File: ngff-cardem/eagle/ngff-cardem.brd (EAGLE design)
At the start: 90 x 100 mm, 150 parts, among them IC1 FPF2109, IC2 FPF2109, IC201 CB3Q3244PW, IC202 CB3Q3244PW, IC203 IP4234CZ6, IC3 TPS22958N-DGK, IC302 TPS22958N-DGN, J301 PJ-002BH-SMT-TR, M2 MENTOR_12701001, M3 MENTOR_12701001, Q201 12MHz, T1 BC847, T101 BC847, U201 IP4234CZ6, U202 AT91SAM3S-AU, U301 MIC5366-1.8YC5, X1 PINHD-2X3-SP, X102 ZX360D-B-10P(30), X2 171826-4-RA, X201 MINI-USB-SHIELD-UX60-MB-5ST, X202 2.54mm, X3 JACK2.5_SJ-2523

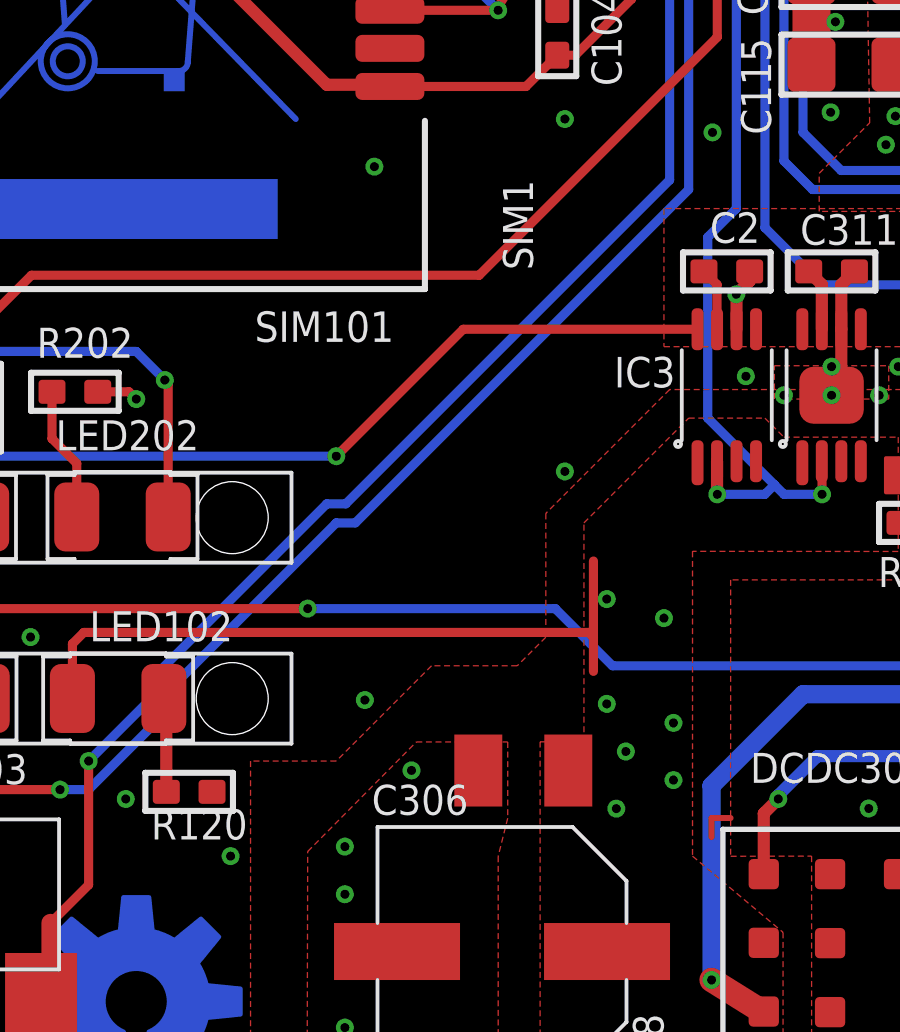
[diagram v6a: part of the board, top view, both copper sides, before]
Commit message: ngff-cardem: a few more GND vias
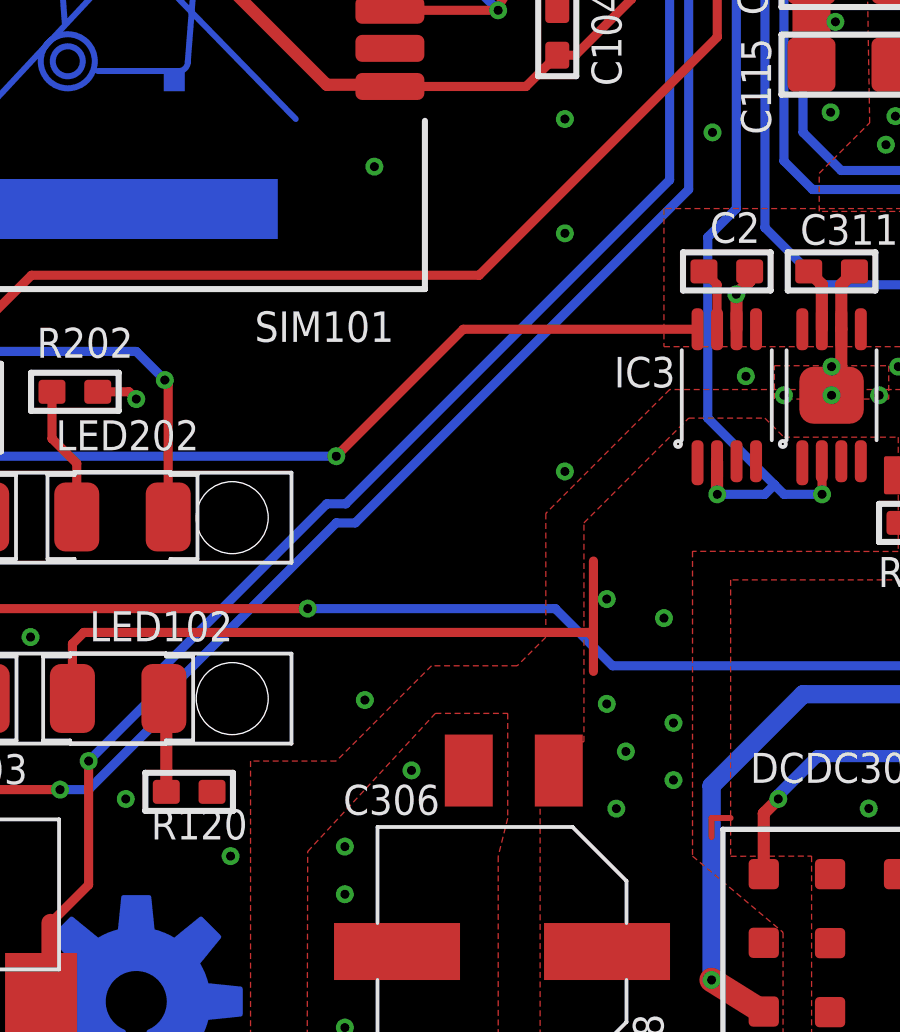
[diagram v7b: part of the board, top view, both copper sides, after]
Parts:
- moved C306 0.32 mm to (27.2, 18.1)
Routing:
- net GND: vias 319 -> 320
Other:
- board text removed: "SIM1"
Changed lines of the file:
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@@
 <text x="80.0405" y="67.05725" size="1" layer="25" font="vector" ratio="16" rot="R180">!RESET</text>
 <text x="80.4215" y="73.02625" size="1" layer="25" font="vector" ratio="16" rot="R180">!W_DIS</text>
-<text x="26.83" y="37.7825" size="1" layer="25" ratio="16" rot="R270">SIM1</text>
 <text x="81.0565" y="75.09" size="1" layer="25" font="vector" ratio="16" rot="R180">PWR_ON</text>
 <text x="80.4215" y="70.01" size="1" layer="25" font="vector" ratio="16" rot="R180">!GPS_DIS</text>
@@
 <attribute name="LINK" value="https://www.digikey.de/product-detail/de/yageo/CC0603KRX7R7BB104/311-1088-1-ND/" x="28.63875" y="42.70375" size="1.778" layer="27" rot="R90" display="off"/>
 </element>
-<element name="C306" library="rcl" package="SMC_B" value="DNP" x="27.506875" y="18.0975" smashed="yes" rot="R180">
-<attribute name="NAME" x="25.674375" y="17.62125" size="1" layer="25" ratio="14" rot="R180"/>
-<attribute name="VALUE" x="29.411875" y="20.6375" size="1" layer="27" ratio="11" rot="R180"/>
-<attribute name="DESCRIPTION" value="CAP TANT 100UF 6.3V 20% 1210" x="27.506875" y="18.0975" size="1.778" layer="27" rot="R180" display="off"/>
-<attribute name="MANUFACTURER" value="AVX Corporation" x="27.506875" y="18.0975" size="1.778" layer="27" rot="R180" display="off"/>
-<attribute name="MANUFACTURERPARTNUMBER" value="F920J107MBA" x="27.506875" y="18.0975" size="1.778" layer="27" rot="R180" display="off"/>
-<attribute name="SOURCE" value="DIGIKEY" x="27.506875" y="18.0975" size="1.778" layer="27" rot="R180" display="off"/>
-<attribute name="SOURCEPARTNUMBER" value="478-8116-1-ND" x="27.506875" y="18.0975" size="1.778" layer="27" rot="R180" display="off"/>
-<attribute name="ROHSCERTIFICATE" value="Bleifrei / RoHS-konform" x="27.506875" y="18.0975" size="1.778" layer="27" rot="R180" display="off"/>
-<attribute name="POPULATED" value="FALSE" x="27.506875" y="18.0975" size="1.778" layer="27" rot="R180" display="off"/>
-<attribute name="CLASS" value="CAPACITOR" x="27.506875" y="18.0975" size="1.778" layer="27" rot="R180" display="off"/>
-<attribute name="LINK" value="http://www.digikey.de/product-detail/de/F920J107MBA/478-8116-1-ND" x="27.506875" y="18.0975" size="1.778" layer="27" rot="R180" display="off"/>
+<element name="C306" library="rcl" package="SMC_B" value="DNP" x="27.189375" y="18.0975" smashed="yes" rot="R180">
+<attribute name="NAME" x="24.721875" y="17.62125" size="1" layer="25" ratio="14" rot="R180"/>
+<attribute name="VALUE" x="29.094375" y="20.6375" size="1" layer="27" ratio="11" rot="R180"/>
+<attribute name="DESCRIPTION" value="CAP TANT 100UF 6.3V 20% 1210" x="27.189375" y="18.0975" size="1.778" layer="27" rot="R180" display="off"/>
+<attribute name="MANUFACTURER" value="AVX Corporation" x="27.189375" y="18.0975" size="1.778" layer="27" rot="R180" display="off"/>
+<attribute name="MANUFACTURERPARTNUMBER" value="F920J107MBA" x="27.189375" y="18.0975" size="1.778" layer="27" rot="R180" display="off"/>
+<attribute name="SOURCE" value="DIGIKEY" x="27.189375" y="18.0975" size="1.778" layer="27" rot="R180" display="off"/>
+<attribute name="SOURCEPARTNUMBER" value="478-8116-1-ND" x="27.189375" y="18.0975" size="1.778" layer="27" rot="R180" display="off"/>
+<attribute name="ROHSCERTIFICATE" value="Bleifrei / RoHS-konform" x="27.189375" y="18.0975" size="1.778" layer="27" rot="R180" display="off"/>
+<attribute name="POPULATED" value="FALSE" x="27.189375" y="18.0975" size="1.778" layer="27" rot="R180" display="off"/>
+<attribute name="CLASS" value="CAPACITOR" x="27.189375" y="18.0975" size="1.778" layer="27" rot="R180" display="off"/>
+<attribute name="LINK" value="http://www.digikey.de/product-detail/de/F920J107MBA/478-8116-1-ND" x="27.189375" y="18.0975" size="1.778" layer="27" rot="R180" display="off"/>
 </element>
 <element name="C301" library="rcl" package="UD-8X10_NICHICON" value="220u / 25V" x="58.32625" y="10.4825" smashed="yes" rot="R270">
@@
 <contactref element="C308" pad="2"/>
 <polygon width="0.3048" layer="1">
-<vertex x="23.94" y="19.05"/>
-<vertex x="26.9875" y="19.05"/>
+<vertex x="24.575" y="20.0025"/>
+<vertex x="26.9875" y="20.0025"/>
 <vertex x="26.9875" y="16.51"/>
 <vertex x="26.67" y="15.24"/>
@@
 <via x="22.225" y="20.4475" extent="1-16" drill="0.3"/>
 <via x="28.8925" y="28.0675" extent="1-16" drill="0.3"/>
+<via x="28.8925" y="36.005" extent="1-16" drill="0.3"/>
 </signal>
 <signal name="MDM_UIM_CLK">

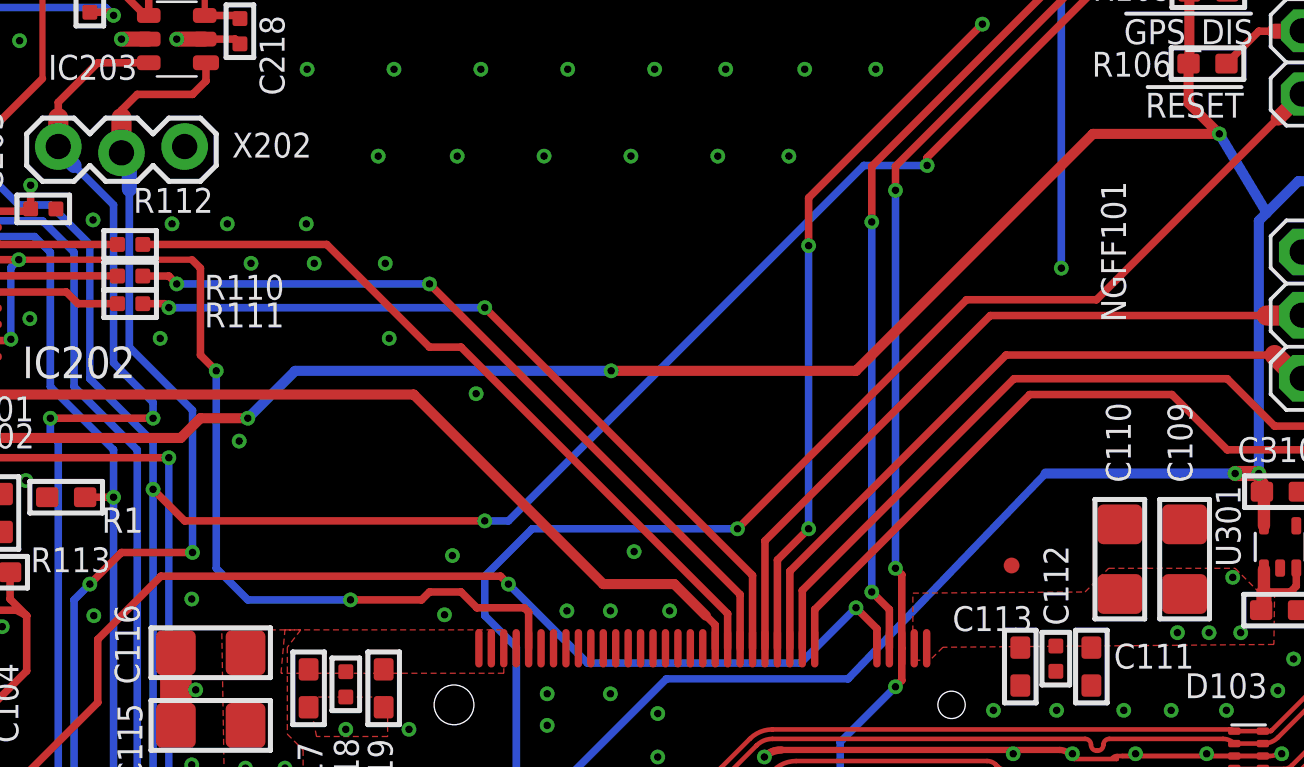
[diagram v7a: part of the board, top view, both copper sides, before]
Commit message: ngff-cardem: improve GND guarding; more GND vias
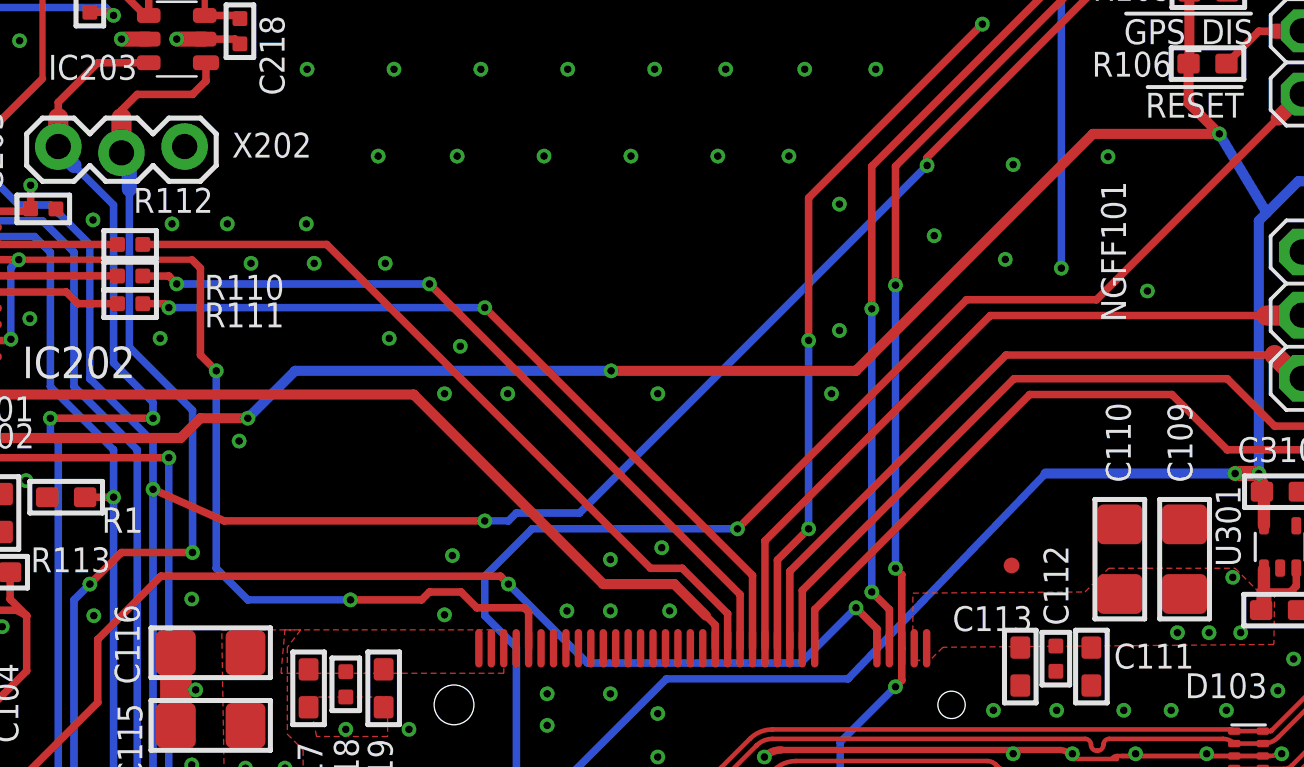
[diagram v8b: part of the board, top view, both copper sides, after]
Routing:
- net GND: vias 320 -> 332
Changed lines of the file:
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@@
 <via x="7.4625" y="69.85" extent="1-16" drill="0.3"/>
 <via x="7.43" y="61.312" extent="1-16" drill="0.3"/>
-<via x="55.53125" y="48.612" extent="1-16" drill="0.3"/>
-<via x="49.18125" y="54.962" extent="1-16" drill="0.3"/>
+<via x="54.57875" y="48.2945" extent="1-16" drill="0.3"/>
+<via x="47.91125" y="54.962" extent="1-16" drill="0.3"/>
 <via x="45.68875" y="57.1845" extent="1-16" drill="0.3"/>
 <via x="42.6725" y="60.20075" extent="1-16" drill="0.3"/>
@@
 <via x="28.8925" y="28.0675" extent="1-16" drill="0.3"/>
 <via x="28.8925" y="36.005" extent="1-16" drill="0.3"/>
+<via x="48.54625" y="56.867" extent="1-16" drill="0.3"/>
+<via x="50.45125" y="54.962" extent="1-16" drill="0.3"/>
+<via x="56.6425" y="48.77075" extent="1-16" drill="0.3"/>
+<via x="56.48375" y="54.962" extent="1-16" drill="0.3"/>
+<via x="63.46875" y="54.962" extent="1-16" drill="0.3"/>
+<via x="67.59625" y="61.312" extent="1-16" drill="0.3"/>
+<via x="70.77125" y="64.1695" extent="1-16" drill="0.3"/>
+<via x="74.58125" y="64.487" extent="1-16" drill="0.3"/>
+<via x="70.45375" y="60.3595" extent="1-16" drill="0.3"/>
+<via x="76.16875" y="59.0895" extent="1-16" drill="0.3"/>
+<via x="63.78625" y="62.582" extent="1-16" drill="0.3"/>
+<via x="63.78625" y="57.502" extent="1-16" drill="0.3"/>
 </signal>
 <signal name="MDM_UIM_CLK">
@@
 <wire x1="65.7935" y1="46.284" x2="65.0875" y2="46.99" width="0.3048" layer="1"/>
 <via x="65.0875" y="46.99" extent="1-16" drill="0.3"/>
-<wire x1="65.0875" y1="46.99" x2="65.0875" y2="61.865" width="0.3048" layer="16"/>
-<via x="65.0875" y="61.865" extent="1-16" drill="0.3"/>
-<wire x1="65.0875" y1="61.865" x2="65.0875" y2="64.1025" width="0.3048" layer="1"/>
+<wire x1="65.0875" y1="46.99" x2="65.0875" y2="58.3725" width="0.3048" layer="16"/>
+<via x="65.0875" y="58.3725" extent="1-16" drill="0.3"/>
+<wire x1="65.0875" y1="58.3725" x2="65.0875" y2="64.1025" width="0.3048" layer="1"/>
 <contactref element="JP1" pad="3"/>
 <wire x1="80.6775" y1="71.7225" x2="81.28" y2="72.0725" width="0.3048" layer="15"/>
@@
 <contactref element="NGFF101" pad="34"/>
 <wire x1="59.2935" y1="44.7275" x2="59.2935" y2="46.1165" width="0.3048" layer="1"/>
-<wire x1="59.2935" y1="46.1165" x2="48.5775" y2="56.8325" width="0.3048" layer="1"/>
-<wire x1="48.5775" y1="56.8325" x2="47.3075" y2="56.8325" width="0.3048" layer="1"/>
-<wire x1="47.3075" y1="56.8325" x2="43.18" y2="60.96" width="0.3048" layer="1"/>
+<wire x1="59.2935" y1="46.1165" x2="57.4675" y2="47.9425" width="0.3048" layer="1"/>
+<wire x1="57.4675" y1="47.9425" x2="56.1975" y2="47.9425" width="0.3048" layer="1"/>
+<wire x1="56.1975" y1="47.9425" x2="43.18" y2="60.96" width="0.3048" layer="1"/>
 <wire x1="43.18" y1="60.96" x2="35.78325" y2="60.96" width="0.3048" layer="1"/>
 <wire x1="35.78325" y1="60.96" x2="35.78225" y2="60.961" width="0.3048" layer="1"/>
@@
 <wire x1="66.2935" y1="47.689" x2="66.04" y2="47.9425" width="0.3048" layer="1"/>
 <via x="66.04" y="47.9425" extent="1-16" drill="0.3"/>
-<wire x1="66.04" y1="47.9425" x2="66.04" y2="63.135" width="0.3048" layer="16"/>
-<via x="66.04" y="63.135" extent="1-16" drill="0.3"/>
-<wire x1="66.04" y1="63.135" x2="66.04" y2="64.1025" width="0.3048" layer="1"/>
+<wire x1="66.04" y1="47.9425" x2="66.04" y2="59.325" width="0.3048" layer="16"/>
+<via x="66.04" y="59.325" extent="1-16" drill="0.3"/>
+<wire x1="66.04" y1="59.325" x2="66.04" y2="64.1025" width="0.3048" layer="1"/>
 <contactref element="T101" pad="C"/>
 <contactref element="C124" pad="1"/>
@@
 <wire x1="61.2935" y1="48.276" x2="62.5475" y2="49.53" width="0.3048" layer="1"/>
 <via x="62.5475" y="49.53" extent="1-16" drill="0.3"/>
-<wire x1="62.5475" y1="49.53" x2="62.5475" y2="60.9125" width="0.3048" layer="16"/>
-<wire x1="62.5475" y1="60.9275" x2="62.5475" y2="60.9125" width="0.3048" layer="16"/>
-<via x="62.5475" y="60.9125" extent="1-16" drill="0.3"/>
-<wire x1="62.5475" y1="60.9125" x2="62.5475" y2="62.8325" width="0.3048" layer="1"/>
+<wire x1="62.5475" y1="49.53" x2="62.5475" y2="57.1025" width="0.3048" layer="16"/>
+<via x="62.5475" y="57.1025" extent="1-16" drill="0.3"/>
+<wire x1="62.5475" y1="57.1025" x2="62.5475" y2="62.8325" width="0.3048" layer="1"/>
 <contactref element="JP1" pad="5"/>
 <wire x1="82.39" y1="69.5475" x2="81.2325" y2="69.5475" width="0.6096" layer="15"/>
@@
 <wire x1="81.28" y1="74.6125" x2="77.47" y2="74.6125" width="0.3048" layer="1"/>
 <wire x1="77.47" y1="74.6125" x2="67.31" y2="64.4525" width="0.3048" layer="1"/>
-<wire x1="37.465" y1="49.8475" x2="36.195" y2="51.1175" width="0.3048" layer="1"/>
-<wire x1="49.53" y1="49.8475" x2="37.465" y2="49.8475" width="0.3048" layer="1"/>
+<wire x1="39.0525" y1="49.8475" x2="36.195" y2="51.1175" width="0.3048" layer="1"/>
+<wire x1="49.53" y1="49.8475" x2="39.0525" y2="49.8475" width="0.3048" layer="1"/>
 <wire x1="50.4825" y1="49.8475" x2="49.53" y2="49.8475" width="0.3048" layer="16"/>
-<wire x1="64.77" y1="64.135" x2="50.4825" y2="49.8475" width="0.3048" layer="16"/>
-<wire x1="67.31" y1="64.135" x2="64.77" y2="64.135" width="0.3048" layer="16"/>
+<wire x1="53.34" y1="50.165" x2="50.8" y2="50.165" width="0.3048" layer="16"/>
+<wire x1="50.8" y1="50.165" x2="50.4825" y2="49.8475" width="0.3048" layer="16"/>
+<wire x1="67.31" y1="64.135" x2="53.34" y2="50.165" width="0.3048" layer="16"/>
 <wire x1="67.31" y1="64.4525" x2="67.31" y2="64.135" width="0.3048" layer="1"/>
 <via x="49.53" y="49.8475" extent="1-16" drill="0.3"/>
